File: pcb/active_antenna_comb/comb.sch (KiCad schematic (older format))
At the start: 0 parts

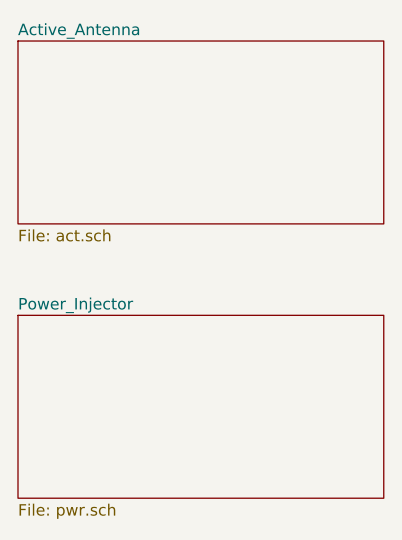
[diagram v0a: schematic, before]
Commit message: v0.5 PCB with 5V DC input
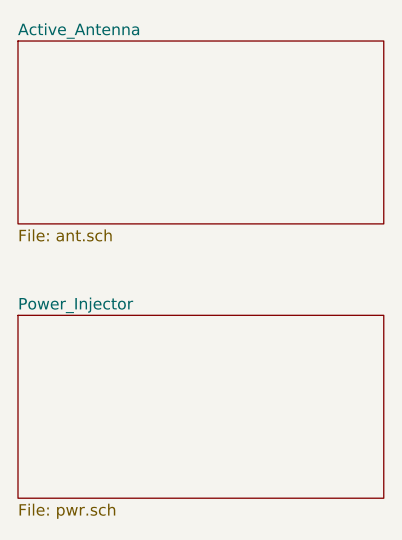
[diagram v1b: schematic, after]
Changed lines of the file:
@@
-EESchema Schematic File Version 2  date Friday, August 07, 2015 01:23:38 PM
+EESchema Schematic File Version 2  date Sunday, January 31, 2016 02:06:10 PM
 LIBS:kiwi
 EELAYER 27 0
@@
 Sheet 1 3
 Title "KiwiSDR - Active Antenna and Power Supply"
-Date "7 aug 2015"
-Rev "1.0"
-Comp "Point Reyes Ventures, LLC"
-Comment1 "August 2015"
+Date "6 sep 2015"
+Rev "1.1"
+Comp ""
+Comment1 "February 2016"
 Comment2 ""
 Comment3 ""
@@
 U 52BC0886
 F0 "Active_Antenna" 50
-F1 "act.sch" 50
+F1 "ant.sch" 50
 $EndSheet
 $Sheet
